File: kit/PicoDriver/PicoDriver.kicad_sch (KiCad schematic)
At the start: 1 part, among them U1 Pico

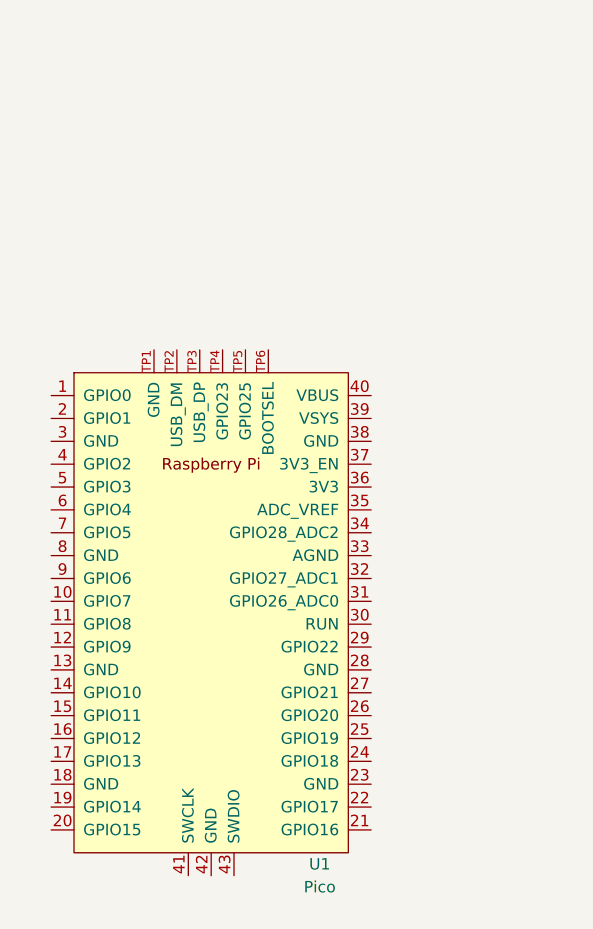
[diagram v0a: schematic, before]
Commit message: add Servo and DC Motor
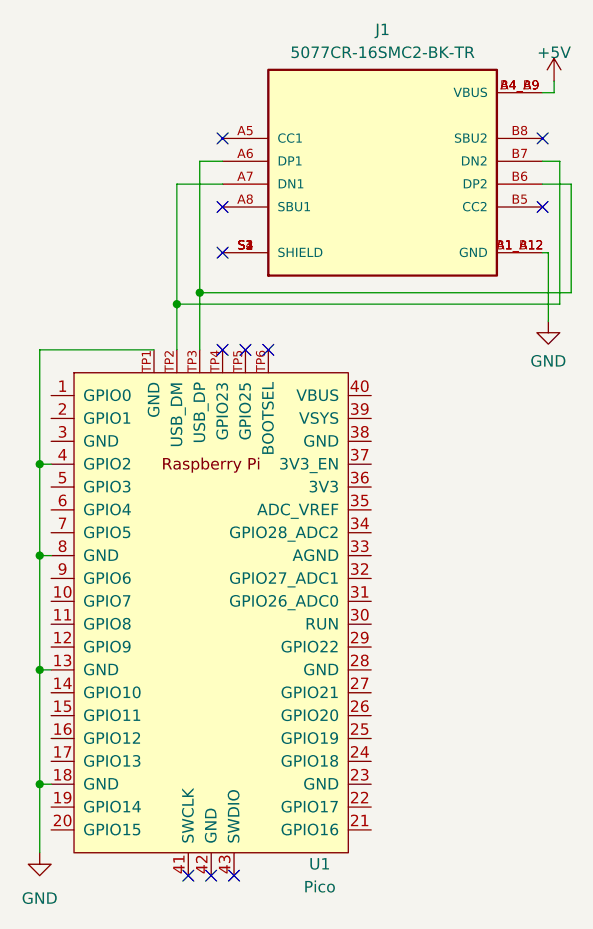
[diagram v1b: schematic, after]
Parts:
- added J1: 5077CR-16SMC2-BK-TR, NELTRON_5077CR-16SMC2-BK-TR, symbol 5077CR-16SMC2-BK-TR:5077CR-16SMC2-BK-TR
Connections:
- net GND: now reaches U1.13 (GND)
- net GND: now also U1.18 (GND), U1.4 (GPIO2), U1.8 (GND), U1.TP1 (GND), J1.A1_B12 (GND), J1.B1_A12 (GND)
- net at U1.TP2 (USB_DM): now also J1.A7 (DN1), J1.B7 (DN2)
- net at U1.TP3 (USB_DP): now also J1.A6 (DP1), J1.B6 (DP2)
- new net: J1.S1 (SHIELD), J1.S2 (SHIELD), J1.S3 (SHIELD), J1.S4 (SHIELD)
- new net +5V: J1.A4_B9 (VBUS), J1.B4_A9 (VBUS)
- no-connect marks 0 -> 11
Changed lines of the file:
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@@
 (kicad_sch (version 20230121) (generator eeschema)
   (paper "A4")
+  (junction (at 64.135 71.12) (diameter 0) (color 0 0 0 0)
+  )
+  (junction (at 81.915 52.07) (diameter 0) (color 0 0 0 0)
+  )
+  (junction (at 79.375 53.34) (diameter 0) (color 0 0 0 0)
+  )
+  (junction (at 64.135 93.98) (diameter 0) (color 0 0 0 0)
+  )
+  (junction (at 64.135 81.28) (diameter 0) (color 0 0 0 0)
+  )
+  (junction (at 64.135 106.68) (diameter 0) (color 0 0 0 0)
+  )
+  (no_connect (at 84.455 58.42))
+  (no_connect (at 84.455 34.925))
+  (no_connect (at 89.535 58.42))
+  (no_connect (at 120.015 42.545))
+  (no_connect (at 83.185 116.84))
+  (no_connect (at 85.725 116.84))
+  (no_connect (at 84.455 42.545))
+  (no_connect (at 120.015 34.925))
+  (no_connect (at 86.995 58.42))
+  (no_connect (at 80.645 116.84))
+  (no_connect (at 84.455 47.625))
+  (wire (pts (xy 79.375 53.34) (xy 121.92 53.34))
+    (stroke (width 0) (type default))
+  )
+  (wire (pts (xy 64.135 93.98) (xy 64.135 81.28))
+    (stroke (width 0) (type default))
+  )
+  (wire (pts (xy 64.135 81.28) (xy 65.405 81.28))
+    (stroke (width 0) (type default))
+  )
+  (wire (pts (xy 81.915 37.465) (xy 84.455 37.465))
+    (stroke (width 0) (type default))
+  )
+  (wire (pts (xy 64.135 93.98) (xy 65.405 93.98))
+    (stroke (width 0) (type default))
+  )
+  (wire (pts (xy 120.015 47.625) (xy 120.65 47.625))
+    (stroke (width 0) (type default))
+  )
+  (wire (pts (xy 120.65 47.625) (xy 120.65 55.245))
+    (stroke (width 0) (type default))
+  )
+  (wire (pts (xy 81.915 52.07) (xy 81.915 37.465))
+    (stroke (width 0) (type default))
+  )
+  (wire (pts (xy 64.135 71.12) (xy 65.405 71.12))
+    (stroke (width 0) (type default))
+  )
+  (wire (pts (xy 121.92 37.465) (xy 121.92 53.34))
+    (stroke (width 0) (type default))
+  )
+  (wire (pts (xy 81.915 58.42) (xy 81.915 52.07))
+    (stroke (width 0) (type default))
+  )
+  (wire (pts (xy 120.015 29.845) (xy 121.285 29.845))
+    (stroke (width 0) (type default))
+  )
+  (wire (pts (xy 79.375 53.34) (xy 79.375 58.42))
+    (stroke (width 0) (type default))
+  )
+  (wire (pts (xy 84.455 40.005) (xy 79.375 40.005))
+    (stroke (width 0) (type default))
+  )
+  (wire (pts (xy 79.375 40.005) (xy 79.375 53.34))
+    (stroke (width 0) (type default))
+  )
+  (wire (pts (xy 81.915 52.07) (xy 123.19 52.07))
+    (stroke (width 0) (type default))
+  )
+  (wire (pts (xy 123.19 40.005) (xy 123.19 52.07))
+    (stroke (width 0) (type default))
+  )
+  (wire (pts (xy 120.015 40.005) (xy 123.19 40.005))
+    (stroke (width 0) (type default))
+  )
+  (wire (pts (xy 64.135 58.42) (xy 76.835 58.42))
+    (stroke (width 0) (type default))
+  )
+  (wire (pts (xy 64.135 81.28) (xy 64.135 71.12))
+    (stroke (width 0) (type default))
+  )
+  (wire (pts (xy 120.015 37.465) (xy 121.92 37.465))
+    (stroke (width 0) (type default))
+  )
+  (wire (pts (xy 64.135 71.12) (xy 64.135 58.42))
+    (stroke (width 0) (type default))
+  )
+  (wire (pts (xy 121.285 29.845) (xy 121.285 28.575))
+    (stroke (width 0) (type default))
+  )
+  (wire (pts (xy 64.135 106.68) (xy 64.135 93.98))
+    (stroke (width 0) (type default))
+  )
+  (wire (pts (xy 64.135 106.68) (xy 65.405 106.68))
+    (stroke (width 0) (type default))
+  )
+  (wire (pts (xy 64.135 106.68) (xy 64.135 114.3))
+    (stroke (width 0) (type default))
+  )
+  (symbol (lib_id "power:+5V") (at 121.285 28.575 0) (unit 1)
+    (in_bom yes) (on_board yes) (dnp no) (fields_autoplaced)
+    (property "Reference" "#PWR01" (at 121.285 32.385 0)
+      (effects (font (size 1.27 1.27)) hide)
+    )
+    (property "Value" "+5V" (at 121.285 25.4 0)
+      (effects (font (size 1.27 1.27)))
+    )
+    (property "Footprint" "" (at 121.285 28.575 0)
+      (effects (font (size 1.27 1.27)) hide)
+    )
+    (property "Datasheet" "" (at 121.285 28.575 0)
+      (effects (font (size 1.27 1.27)) hide)
+    )
+    (pin "1")
+    (instances
+      (project "PicoDriver"
+        (path "/49df2efe-f108-4601-87fa-93951654c14a"
+          (reference "#PWR01") (unit 1)
+        )
+      )
+    )
+  )
+  (symbol (lib_id "power:GND") (at 120.65 55.245 0) (unit 1)
+    (in_bom yes) (on_board yes) (dnp no) (fields_autoplaced)
+    (property "Reference" "#PWR02" (at 120.65 61.595 0)
+      (effects (font (size 1.27 1.27)) hide)
+    )
+    (property "Value" "GND" (at 120.65 59.69 0)
+      (effects (font (size 1.27 1.27)))
+    )
+    (property "Footprint" "" (at 120.65 55.245 0)
+      (effects (font (size 1.27 1.27)) hide)
+    )
+    (property "Datasheet" "" (at 120.65 55.245 0)
+      (effects (font (size 1.27 1.27)) hide)
+    )
+    (pin "1")
+    (instances
+      (project "PicoDriver"
+        (path "/49df2efe-f108-4601-87fa-93951654c14a"
+          (reference "#PWR02") (unit 1)
+        )
+      )
+    )
+  )
+  (symbol (lib_id "power:GND") (at 64.135 114.3 0) (unit 1)
+    (in_bom yes) (on_board yes) (dnp no) (fields_autoplaced)
+    (property "Reference" "#PWR03" (at 64.135 120.65 0)
+      (effects (font (size 1.27 1.27)) hide)
+    )
+    (property "Value" "GND" (at 64.135 119.38 0)
+      (effects (font (size 1.27 1.27)))
+    )
+    (property "Footprint" "" (at 64.135 114.3 0)
+      (effects (font (size 1.27 1.27)) hide)
+    )
+    (property "Datasheet" "" (at 64.135 114.3 0)
+      (effects (font (size 1.27 1.27)) hide)
+    )
+    (pin "1")
+    (instances
+      (project "PicoDriver"
+        (path "/49df2efe-f108-4601-87fa-93951654c14a"
+          (reference "#PWR03") (unit 1)
+        )
+      )
+    )
+  )
+  (symbol (lib_id "5077CR-16SMC2-BK-TR:5077CR-16SMC2-BK-TR") (at 102.235 37.465 0) (unit 1)
+    (in_bom yes) (on_board yes) (dnp no) (fields_autoplaced)
+    (property "Reference" "J1" (at 102.235 22.86 0)
+      (effects (font (size 1.27 1.27)))
+    )
+    (property "Value" "5077CR-16SMC2-BK-TR" (at 102.235 25.4 0)
+      (effects (font (size 1.27 1.27)))
+    )
+    (property "Footprint" "NELTRON_5077CR-16SMC2-BK-TR" (at 102.235 37.465 0)
+      (effects (font (size 1.27 1.27)) (justify bottom) hide)
+    )
+    (property "Datasheet" "" (at 102.235 37.465 0)
+      (effects (font (size 1.27 1.27)) hide)
+    )
+    (property "PARTREV" "B" (at 102.235 37.465 0)
+      (effects (font (size 1.27 1.27)) (justify bottom) hide)
+    )
+    (property "SNAPEDA_PN" "5077CR-16SMC2-BK-TR" (at 102.235 37.465 0)
+      (effects (font (size 1.27 1.27)) (justify bottom) hide)
+    )
+    (property "STANDARD" "Manufacturer Recommendations" (at 102.235 37.465 0)
+      (effects (font (size 1.27 1.27)) (justify bottom) hide)
+    )
+    (property "MAXIMUM_PACKAGE_HEIGHT" "3.26mm" (at 102.235 37.465 0)
+      (effects (font (size 1.27 1.27)) (justify bottom) hide)
+    )
+    (property "MANUFACTURER" "Neltron" (at 102.235 37.465 0)
+      (effects (font (size 1.27 1.27)) (justify bottom) hide)
+    )
+    (pin "A1_B12")
+    (pin "A4_B9")
+    (pin "A5")
+    (pin "A6")
+    (pin "A7")
+    (pin "A8")
+    (pin "B1_A12")
+    (pin "B4_A9")
+    (pin "B5")
+    (pin "B6")
+    (pin "B7")
+    (pin "B8")
+    (pin "S1")
+    (pin "S2")
+    (pin "S3")
+    (pin "S4")
+    (instances
+      (project "PicoDriver"
+        (path "/49df2efe-f108-4601-87fa-93951654c14a"
+          (reference "J1") (unit 1)
+        )
+      )
+    )
+  )
   (symbol (lib_id "RPi_Pico:Pico") (at 83.185 87.63 0) (unit 1)
     (in_bom yes) (on_board yes) (dnp no)

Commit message: change
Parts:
- added C1, C2: 2.2µ, symbol Device:C
- added C3, C6, C7, C8: 10µ, symbol Device:C_Polarized
- added C4, C5: 0.01µ, symbol Device:C
- added J10: LeftMotor, symbol Connector:Conn_01x02_Socket
- added J11: Servo, symbol Connector:Conn_01x03_Socket
- added J12: FR_ESC, symbol Connector:Conn_01x03_Socket
- added J13: RR_ESC, symbol Connector:Conn_01x03_Socket
- added J14: FL_ESC, symbol Connector:Conn_01x03_Socket
- added J15: RL_ESC, symbol Connector:Conn_01x03_Socket
- added J16: Micro_SD_Card, symbol Connector:Micro_SD_Card
- added J2: FLED_Blue, symbol Connector:Conn_01x02_Socket
- added J3: FLED_Red, symbol Connector:Conn_01x02_Socket
- added J4: OLED, symbol Connector:Conn_01x07_Socket
- added J5: AudioJack3, symbol Connector_Audio:AudioJack3
- added J6: 9DoF, symbol Connector:Conn_01x04_Socket
- added J7: Temperature, symbol Connector:Conn_01x04_Socket
- added J8: UltraSonic, symbol Connector:Conn_01x04_Socket
- added J9: RightMotor, symbol Connector:Conn_01x02_Socket
- added Q1, Q2: 2SC1815, Package_TO_SOT_THT:TO-92_Inline, symbol Transistor_BJT:2SC1815
- added R1, R2: 10k, symbol Device:R
- added R3, R5, R6: 1k, symbol Device:R
- added R4: 2k, symbol Device:R
- added U2: PCM5102A, PCM5102A:PCM5102A_DIP, symbol Audio:PCM5102A
- added U3: TC78H653FTG,EL, Package_DIP:DIP-16_W7.62mm, symbol TC78H653FTG_EL:TC78H653FTG,EL
- J1: footprint NELTRON_5077CR-16SMC2-BK-TR -> NELTRON_5077CR-16SMC2-BK-TR:NELTRON_5077CR-16SMC2-BK-TR
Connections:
- net +5V: now also U1.39 (VSYS), U1.40 (VBUS), J11.2 (Pin_2), J12.2 (Pin_2), J13.2 (Pin_2), J14.2 (Pin_2), J15.2 (Pin_2), J2.1 (Pin_1), J3.1 (Pin_1), J8.1 (Pin_1), U3.15 (VM), U3.16 (VM), U3.2 (MODE), U3.3 (STBY)
- net GND: now also U1.23 (GND), U1.28 (GND), U1.3 (GND), U1.38 (GND), C2.2, C3.2, C4.2, C5.2, C6.2, C7.2, C8.2, J11.3 (Pin_3), J12.3 (Pin_3), J13.3 (Pin_3), J14.3 (Pin_3), J15.3 (Pin_3), J16.6 (VSS), J16.9 (SHIELD), J4.2 (Pin_2), J5.S, J6.2 (Pin_2), J7.3 (Pin_3), J8.4 (Pin_4), Q1.1 (E), Q2.1 (E), R4.2, U2.10 (DEMP), U2.11 (FLT), U2.12 (SCK), U2.16 (FMT), U2.19 (DGND), U2.3 (CPGND), U2.9 (AGND); no longer U1.4 (GPIO2)
- net GP7: now reaches U1.10 (GPIO7)
- net GP7: now also J11.1 (Pin_1)
- net GP8: now reaches U1.11 (GPIO8)
- net GP8: now also J4.7 (Pin_7)
- net GP9: now reaches U1.12 (GPIO9)
- net GP9: now also J4.6 (Pin_6)
- net GP10: now reaches U1.14 (GPIO10)
- net GP10: now also J16.5 (CLK), J4.4 (Pin_4)
- net GP11: now reaches U1.15 (GPIO11)
- net GP11: now also J16.3 (CMD), J4.3 (Pin_3)
- net GP12: now reaches U1.16 (GPIO12)
- net GP12: now also J16.7 (DAT0)
- net GP13: now reaches U1.17 (GPIO13)
- net GP13: now also J4.5 (Pin_5)
- net GP14: now reaches U1.19 (GPIO14)
- net GP14: now also R3.1
- net GP15: now reaches U1.20 (GPIO15)
- net GP15: now also J8.2 (Pin_2)
- net GP16: now reaches U1.21 (GPIO16)
- net GP16: now also J6.3 (Pin_3), J7.2 (Pin_2)
- net GP17: now reaches U1.22 (GPIO17)
- net GP17: now also J6.4 (Pin_4), J7.4 (Pin_4)
- net GP18: now reaches U1.24 (GPIO18)
- net GP18: now also U3.5 (IN3/ENB_B), U3.6 (IN1/ENB_A)
- net GP19: now reaches U1.25 (GPIO19)
- net GP19: now also U2.13 (BCK)
- net GP20: now reaches U1.26 (GPIO20)
- net GP20: now also U2.15 (LRCK)
- net GP21: now reaches U1.27 (GPIO21)
- net GP21: now also U2.14 (DIN)
- net GP22: now reaches U1.29 (GPIO22)
- net GP22: now also U3.7 (IN2/PHA_A)
- net GP26: now reaches U1.31 (GPIO26_ADC0)
- net GP26: now also U3.4 (IN4/PHA_B)
- net GP27: now reaches U1.32 (GPIO27_ADC1)
- net GP27: now also R2.2
- net GP28: now reaches U1.34 (GPIO28_ADC2)
- net GP28: now also R1.2
- net +3.3V: now reaches U1.36 (3V3)
- net +3.3V: now also C6.1, C7.1, C8.1, J16.4 (VDD), J4.1 (Pin_1), J6.1 (Pin_1), J7.1 (Pin_1), U2.1 (CPVDD), U2.17 (XSMT), U2.20 (DVDD), U2.8 (AVDD)
- net GP3: now reaches U1.5 (GPIO3)
- net GP3: now also J13.1 (Pin_1)
- net GP4: now reaches U1.6 (GPIO4)
- net GP4: now also J14.1 (Pin_1)
- net GP5: now reaches U1.7 (GPIO5)
- net GP5: now also J15.1 (Pin_1)
- net GP6: now reaches U1.9 (GPIO6)
- net GP6: now also J16.2 (DAT3/CD)
- new net: C3.1, U2.18 (LDOO)
- new net: J9.1 (Pin_1), U3.14 (OUT4)
- new net: J9.2 (Pin_2), U3.13 (OUT3)
- new net: J10.1 (Pin_1), U3.12 (OUT1)
- new net: J10.2 (Pin_2), U3.11 (OUT2)
- new net: J2.2 (Pin_2), Q1.2 (C)
- new net: Q1.3 (B), R1.1
- new net: J8.3 (Pin_3), R3.2, R4.1
- new net: C1.1, U2.2 (CAPP)
- new net: C1.2, U2.4 (CAPM)
- new net: C2.1, U2.5 (VNEG)
- new net: R6.1, U2.6 (OUTL)
- new net: R5.1, U2.7 (OUTR)
- new net: C4.1, J5.T, R6.2
- new net: U3.1 (LARGE), U3.10 (GND), U3.8 (GND), U3.9 (GND)
- new net: C5.1, J5.R, R5.2
- new net: J3.2 (Pin_2), Q2.2 (C)
- new net: Q2.3 (B), R2.1
- new net GP2: J12.1 (Pin_1), U1.4 (GPIO2)
- no-connect marks 11 -> 19
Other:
- note added: "LEDs&Display"
- note added: "Motors"
- note added: "Sensors"
- note added: "Sound"
- moved on the sheet: J1, U1

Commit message: fix sch
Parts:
- removed J11: Servo, symbol Connector:Conn_01x03_Socket
- removed J12: FR_ESC, symbol Connector:Conn_01x03_Socket
- removed J13: RR_ESC, symbol Connector:Conn_01x03_Socket
- removed J14: FL_ESC, symbol Connector:Conn_01x03_Socket
- removed J15: RL_ESC, symbol Connector:Conn_01x03_Socket
- added J11: Servo, symbol Connector:Conn_01x03_Pin
- added J12: FR_ESC, symbol Connector:Conn_01x03_Pin
- added J13: RR_ESC, symbol Connector:Conn_01x03_Pin
- added J14: FL_ESC, symbol Connector:Conn_01x03_Pin
- added J15: RL_ESC, symbol Connector:Conn_01x03_Pin
- added J17: Lipo_In, symbol Connector:Conn_01x02_Socket
- added J18: FR_PW, symbol Connector:Conn_01x02_Pin
- added J19: RR_PW, symbol Connector:Conn_01x02_Pin
- added J20: FL_PW, symbol Connector:Conn_01x02_Pin
- added J21: RL_PW, symbol Connector:Conn_01x02_Pin
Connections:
- net +5V: now also J11.2 (Pin_2), J12.2 (Pin_2), J13.2 (Pin_2), J14.2 (Pin_2), J15.2 (Pin_2)
- net GND: now also U3.1 (LARGE), U3.10 (GND), U3.8 (GND), U3.9 (GND), J11.3 (Pin_3), J12.3 (Pin_3), J13.3 (Pin_3), J14.3 (Pin_3), J15.3 (Pin_3), J17.2 (Pin_2), J18.2 (Pin_2), J19.2 (Pin_2), J20.2 (Pin_2), J21.2 (Pin_2)
- net GP14: now also R3.2, R4.1; no longer R3.1
- net GP2: now also J12.1 (Pin_1)
- net GP3: now also J13.1 (Pin_1)
- net GP4: now also J14.1 (Pin_1)
- net GP5: now also J15.1 (Pin_1)
- net GP7: now also J11.1 (Pin_1)
- new net: J8.3 (Pin_3), R3.1
- new net +12V: J17.1 (Pin_1), J18.1 (Pin_1), J19.1 (Pin_1), J20.1 (Pin_1), J21.1 (Pin_1)
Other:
- moved on the sheet: R3, R4
